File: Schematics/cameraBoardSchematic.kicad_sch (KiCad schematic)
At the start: 0 parts

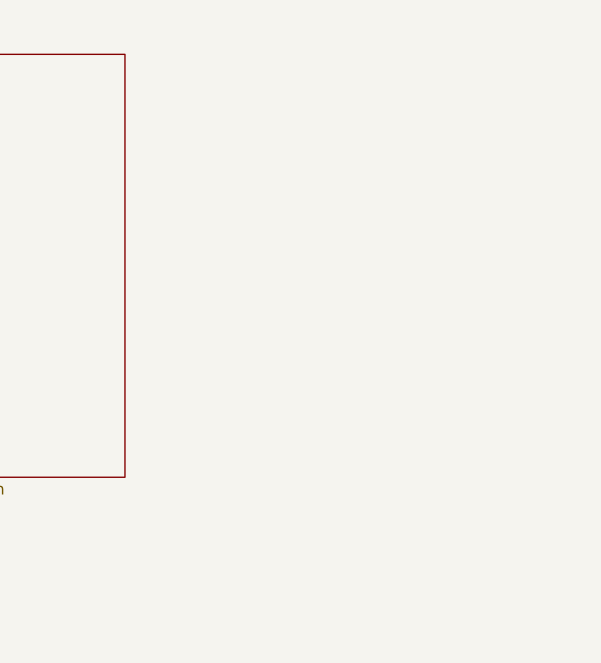
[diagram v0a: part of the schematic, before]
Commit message: added usb type C and changed to CAN2
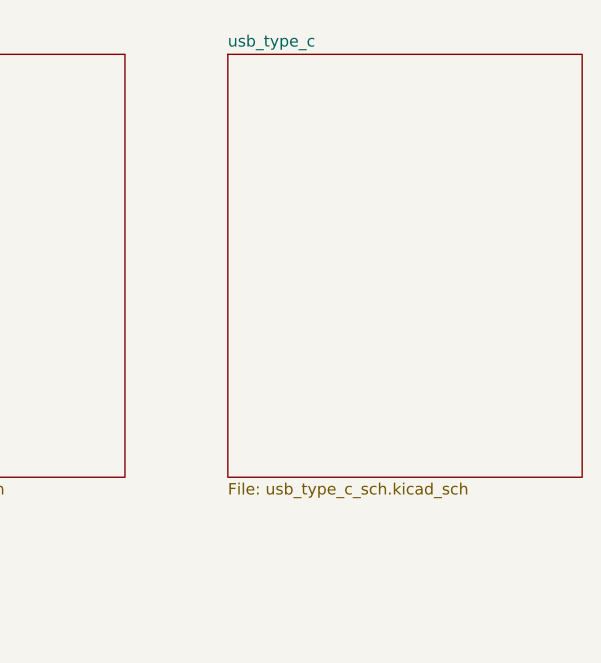
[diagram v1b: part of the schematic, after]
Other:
- added sheet usb_type_c (usb_type_c_sch.kicad_sch)
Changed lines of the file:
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@@
+	)
+	(sheet
+		(at 158.75 19.05)
+		(size 39.37 46.99)
+		(exclude_from_sim no)
+		(in_bom yes)
+		(on_board yes)
+		(dnp no)
+		(fields_autoplaced yes)
+		(stroke
+			(width 0.1524)
+			(type solid)
+		)
+		(fill
+			(color 0 0 0 0.0000)
+		)
+		(property "Sheetname" "usb_type_c"
+			(at 158.75 18.3384 0)
+			(effects
+				(font
+					(size 1.27 1.27)
+				)
+				(justify left bottom)
+			)
+		)
+		(property "Sheetfile" "usb_type_c_sch.kicad_sch"
+			(at 158.75 66.6246 0)
+			(effects
+				(font
+					(size 1.27 1.27)
+				)
+				(justify left top)
+			)
+		)
+		(instances
+			(project "cameraBoardSchematic"
+				(path "/65068a32-f105-4204-b50e-234054c5a6d0"
+					(page "8")
+				)
+			)
+		)
 	)
 	(sheet
